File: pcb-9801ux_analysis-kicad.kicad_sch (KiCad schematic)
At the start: 1 part, among them U1 YM2203C

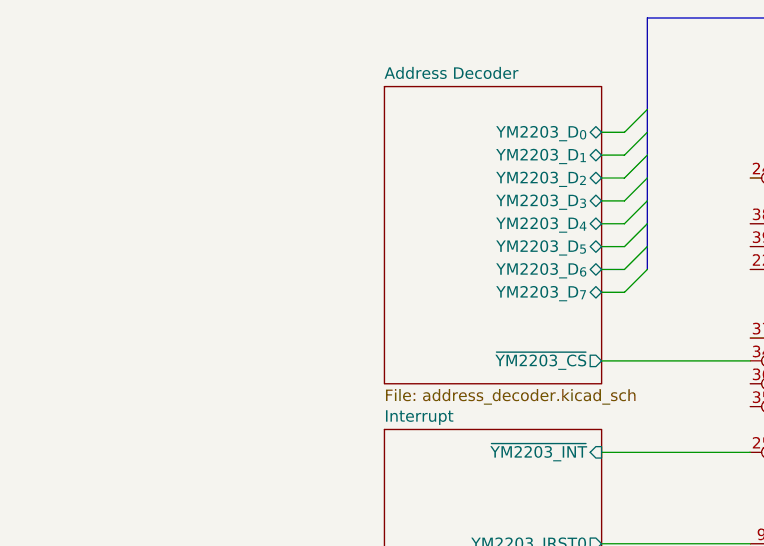
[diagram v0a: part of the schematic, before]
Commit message: Add even more pins
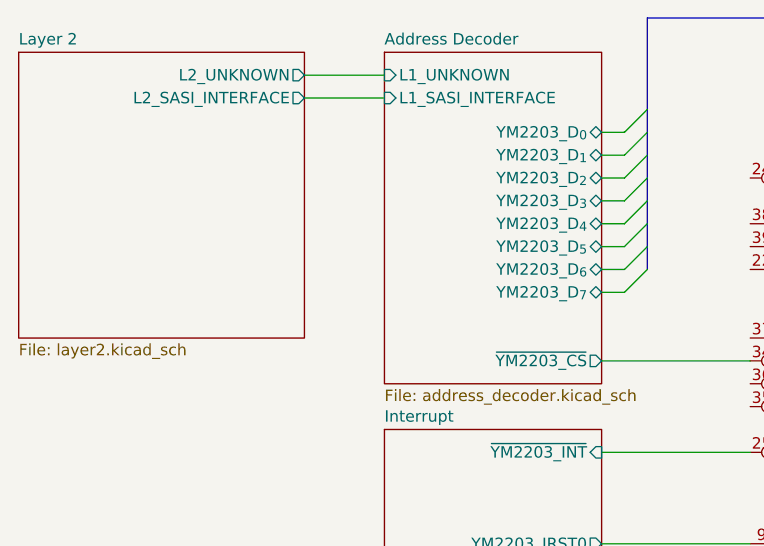
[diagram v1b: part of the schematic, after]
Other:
- added sheet Layer 2 (layer2.kicad_sch)
- sheet Address Decoder ports: added L1_SASI_INTERFACE, L1_UNKNOWN; removed none
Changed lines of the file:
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@@
+	(wire
+		(pts
+			(xy 49.53 25.4) (xy 58.42 25.4)
+		)
+		(stroke
+			(width 0)
+			(type default)
+		)
+	)
 	(wire
 		(pts
@@
 		(pts
 			(xy 82.55 77.47) (xy 99.06 77.47)
+		)
+		(stroke
+			(width 0)
+			(type default)
+		)
+	)
+	(wire
+		(pts
+			(xy 49.53 27.94) (xy 58.42 27.94)
 		)
 		(stroke
@@
 	)
 	(sheet
-		(at 58.42 26.67)
-		(size 24.13 33.02)
+		(at 58.42 22.86)
+		(size 24.13 36.83)
 		(exclude_from_sim no)
 		(in_bom yes)
@@
 		)
 		(property "Sheetname" "Address Decoder"
-			(at 58.42 25.9584 0)
+			(at 58.42 22.1484 0)
 			(effects
 				(font
@@
 				)
 				(justify right)
+			)
+		)
+		(pin "L1_UNKNOWN" input
+			(at 58.42 25.4 180)
+			(effects
+				(font
+					(size 1.27 1.27)
+				)
+				(justify left)
+			)
+		)
+		(pin "L1_SASI_INTERFACE" input
+			(at 58.42 27.94 180)
+			(effects
+				(font
+					(size 1.27 1.27)
+				)
+				(justify left)
 			)
 		)
@@
 				)
 			)
+		)
+	)
+	(sheet
+		(at 17.78 22.86)
+		(size 31.75 31.75)
+		(exclude_from_sim no)
+		(in_bom yes)
+		(on_board yes)
+		(dnp no)
+		(fields_autoplaced yes)
+		(stroke
+			(width 0.1524)
+			(type solid)
+		)
+		(fill
+			(color 0 0 0 0.0000)
+		)
+		(property "Sheetname" "Layer 2"
+			(at 17.78 22.1484 0)
+			(effects
+				(font
+					(size 1.27 1.27)
+				)
+				(justify left bottom)
+			)
+		)
+		(property "Sheetfile" "layer2.kicad_sch"
+			(at 17.78 55.1946 0)
+			(effects
+				(font
+					(size 1.27 1.27)
+				)
+				(justify left top)
+			)
+		)
+		(pin "L2_SASI_INTERFACE" output
+			(at 49.53 27.94 0)
+			(effects
+				(font
+					(size 1.27 1.27)
+				)
+				(justify right)
+			)
+		)
+		(pin "L2_UNKNOWN" output
+			(at 49.53 25.4 0)
+			(effects
+				(font
+					(size 1.27 1.27)
+				)
+				(justify right)
+			)
+		)
+		(instances
+			(project "pcb-9801ux_analysis-kicad"
+				(path "/e1c751df-dbb0-421f-aa76-3a1992ed5601"
+					(page "4")
+				)
+			)

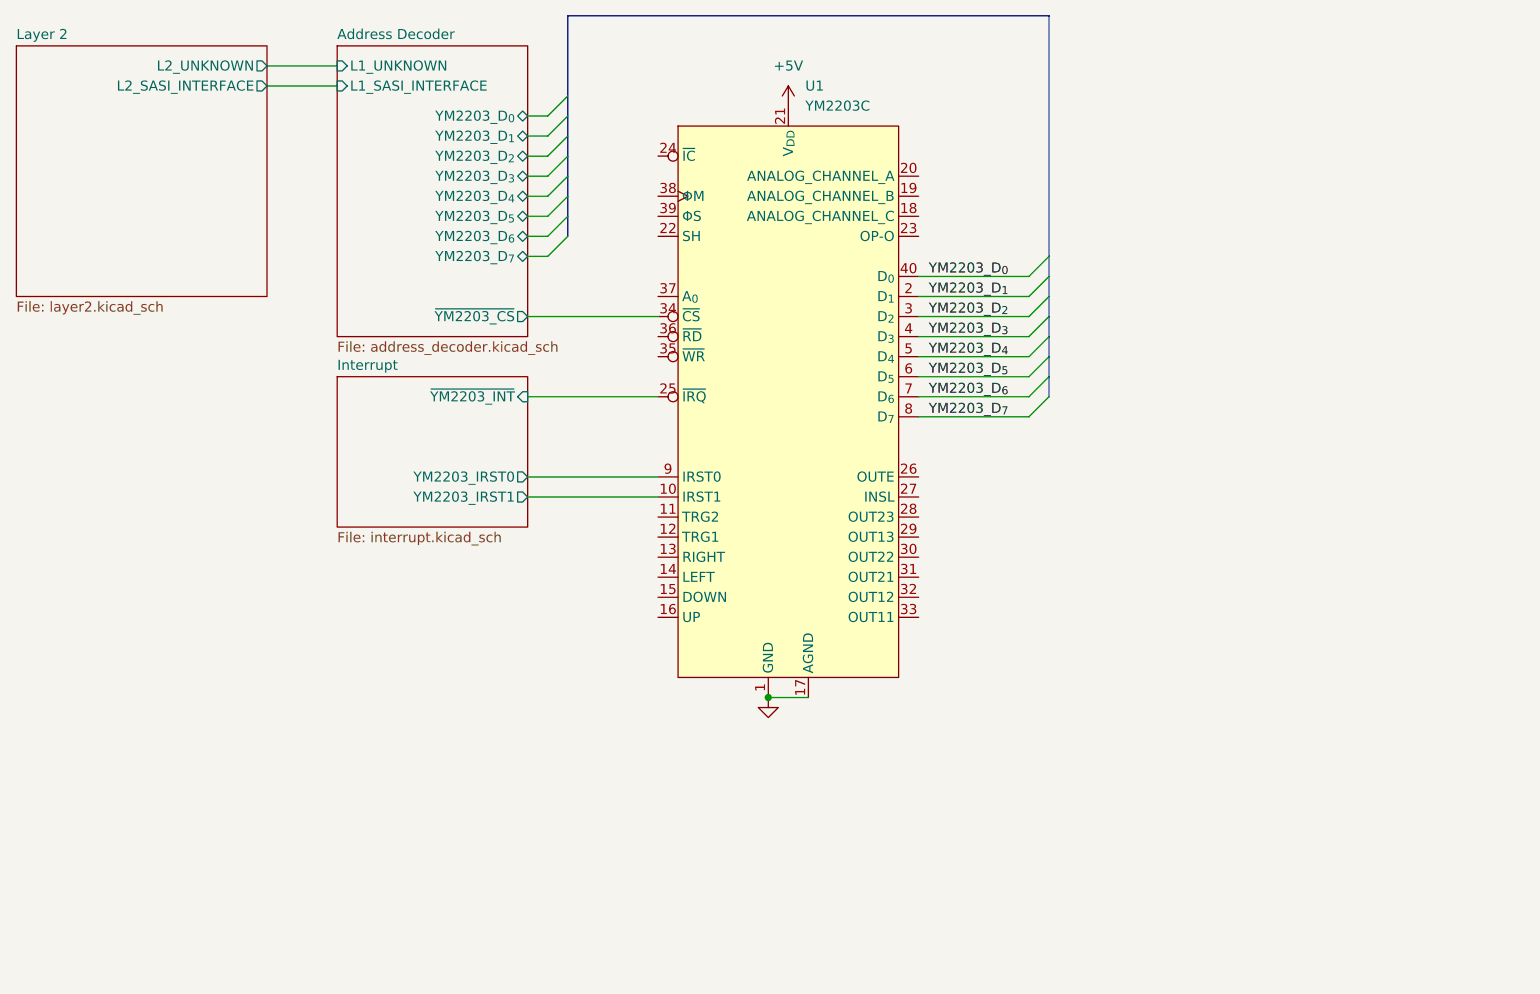
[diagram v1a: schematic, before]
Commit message: Add address decoder description
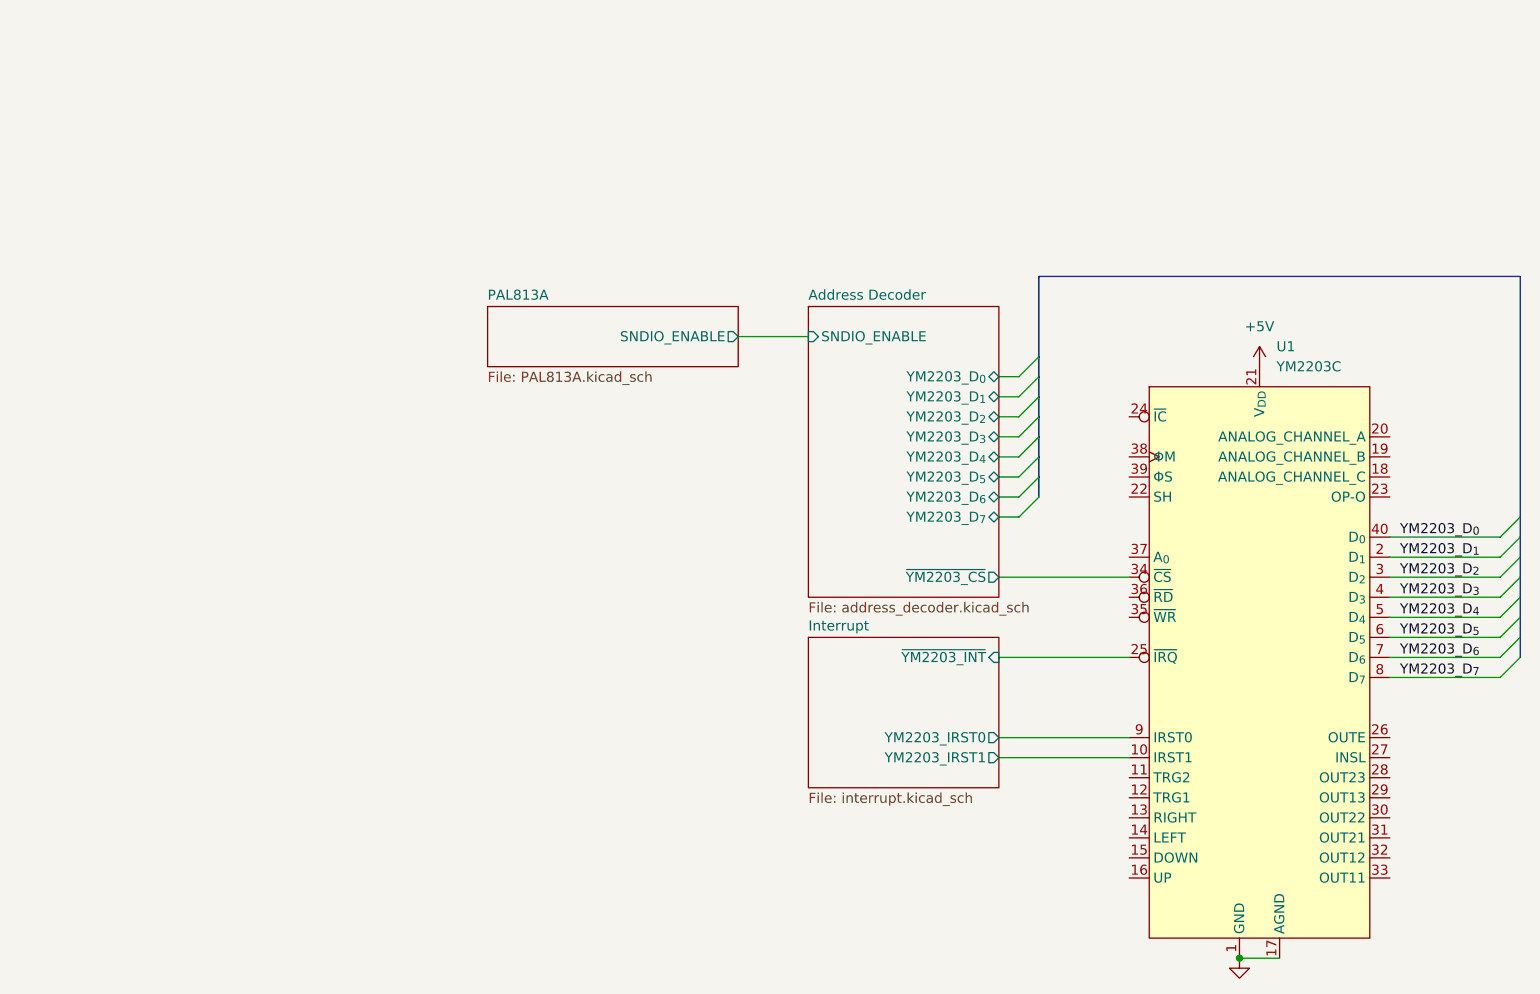
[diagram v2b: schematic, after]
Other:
- sheet Layer 2 renamed PAL813A
- sheet Address Decoder ports: added SNDIO_ENABLE; removed L1_SASI_INTERFACE, L1_UNKNOWN
- sheet PAL813A: file layer2.kicad_sch -> PAL813A.kicad_sch
- sheet PAL813A ports: added SNDIO_ENABLE; removed L2_SASI_INTERFACE, L2_UNKNOWN
- moved on the sheet: U1
